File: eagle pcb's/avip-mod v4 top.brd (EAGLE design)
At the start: 70.5 x 13 mm, 28 parts, among them J4 0ohm, U1 14m2, U2 SN74LVC2G17DBV

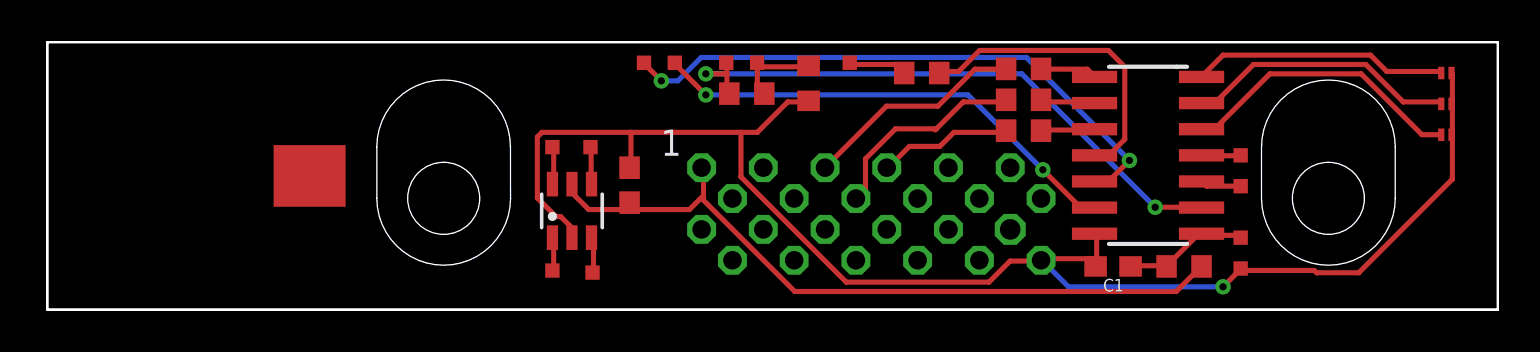
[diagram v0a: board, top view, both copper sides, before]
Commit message: Fix PCB preview and update pictures
Conflict between mill and dimensions layer causing all PCB's to not show up in manufacture preview.
Add pictures of v3, v4 and v4 top PCB.
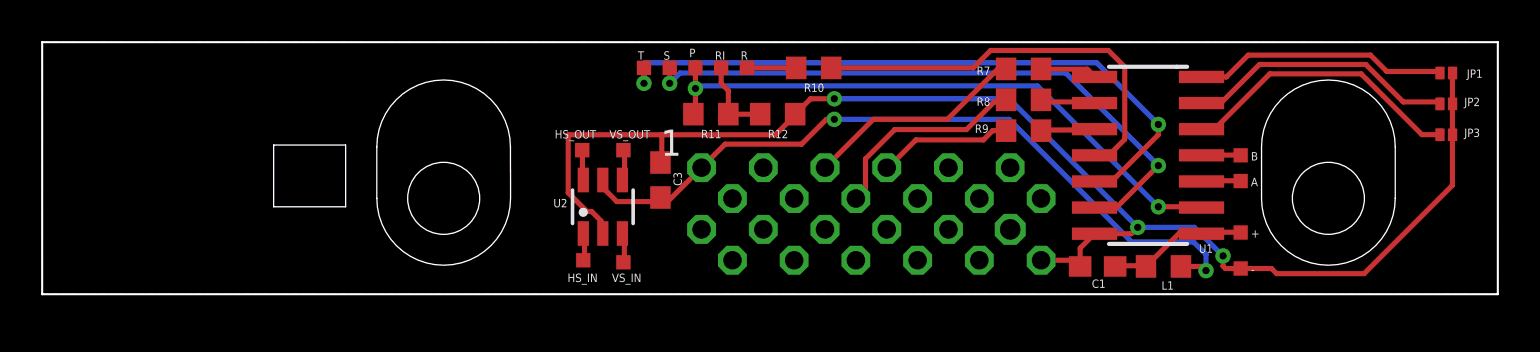
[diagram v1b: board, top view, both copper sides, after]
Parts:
- removed H_SYNC_IN, H_SYNC_OUT, PROG, RESET, RING, SPEAK, TOGGLE, VCC2, V_SYNC_IN, V_SYNC_OUT: (no value), testpad:TP07SQ
- removed J4: 0ohm, rcl:R0603
- added +, HS_IN, HS_OUT, P, R, RI, S, T, VS_IN, VS_OUT: (no value), testpad:TP07SQ
- added L1: 0ohm, rcl:R0603
- moved R10 5.26 mm to (44.2, 19.2)
- moved R12 2.12 mm to (42.5, 17.0), turned to 180 degrees
- moved R11 2.02 mm to (39.2, 17.0)
- moved C3 1.52 mm to (36.8, 13.8)
- moved U2 1.51 mm to (34.0, 12.5)
- moved C1 0.75 mm to (58.0, 9.60)
- moved A 0.25 mm to (65.0, 13.8)
- turned JP1 to 0 degrees
- turned JP2 to 0 degrees
- turned JP3 to 0 degrees
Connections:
- net H_SYNC_IN: now also HS_IN.TP; no longer H_SYNC_IN.TP
- net H_SYNC_OUT: now also HS_OUT.TP; no longer H_SYNC_OUT.TP
- net PROG: now also P.TP; no longer PROG.TP
- net RESET: now also R.TP; no longer RESET.TP
- net RING: now also RI.TP; no longer RING.TP
- net SPEAK: now also S.TP; no longer SPEAK.TP
- net TOGGLE: now also T.TP; no longer TOGGLE.TP
- net VCC: now also L1.2; no longer J4.2
- net VDD: now also +.TP, L1.1; no longer J4.1, VCC2.TP
- net V_SYNC_IN: now also VS_IN.TP; no longer V_SYNC_IN.TP
- net V_SYNC_OUT: now also VS_OUT.TP; no longer V_SYNC_OUT.TP
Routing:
- net SPEAK: track 23.3 -> 31.2 mm
- net GND: track 73.5 -> 68.3 mm, vias 1 -> 3
- net RESET_PROT: track 15.1 -> 20.3 mm
- net TOGGLE: track 28.6 -> 32.5 mm
- net VCC: track 36.1 -> 37.0 mm, vias 0 -> 2
- net VDD: track 6.18 -> 6.91 mm
- net PROG: track 29.4 -> 30.0 mm
- added copper zone on layer 1, net GND
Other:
- board size 70.5 x 13 mm -> 70.8 x 12.2 mm
- board text added: "+"
- board text added: "-"
- board text added: "A"
- board text added: "B"
